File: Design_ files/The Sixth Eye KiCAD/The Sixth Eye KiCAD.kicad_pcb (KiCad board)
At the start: 2 copper layers, 33.5 x 31.6 mm, 13 parts, among them J1 Battery conn, J2 US Sensor conn., J3 Vibration out, U1 ATmega328-AU, U2 LTC3525ISC6-5, Y1 8Mhz

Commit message: Accelrometer pcb
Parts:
- added C5: 2.2uf, Capacitor_Tantalum_SMD:CP_EIA-1608-10_AVX-L, F.Cu at (154.9, 71.9)
- added H2: MountingHole, MountingHole:MountingHole_2mm, F.Cu at (155.7, 65.7)
- added Q1: BC547, Package_TO_SOT_SMD:SOT-23, F.Cu at (148.9, 69.1)
- added R2: 2.2R, Resistor_SMD:R_0603_1608Metric_Pad0.98x0.95mm_HandSolder, F.Cu at (150.2, 74.4)
- added U3: ADXL343, Package_LGA:LGA-14_3x5mm_P0.8mm_LayoutBorder1x6y, F.Cu at (142.6, 68.4)
- added c2: 0.1uf, Capacitor_Tantalum_SMD:CP_EIA-1608-08_AVX-J, F.Cu at (142.4, 64.6)
- moved J2 15.8 mm to (132.4, 67.9), turned to 270 degrees
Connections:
- U1 pad 13: Echo -> Net-(U1-Pad13)
- U1 pad 14: Trig -> ~CS
- U1 pad 15: Net-(U1-Pad15) -> MOSI
- U1 pad 16: Out -> MISO
- U1 pad 17: Net-(U1-Pad17) -> SCK
- U1 pad 23: Net-(U1-Pad23) -> Out
- U1 pad 24: Net-(U1-Pad24) -> Echo
- U1 pad 25: Net-(U1-Pad25) -> Trig
- U1 pad 26: Net-(U1-Pad26) -> VDD_IO
- U1 pad 27: Net-(U1-Pad27) -> INT1
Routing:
- net ~CS: track 0.00 -> 19.8 mm
- net Trig: track 24.0 -> 4.14 mm
- net Net-(U1-Pad13): track 0.00 -> 17.9 mm
- net Echo: track 24.6 -> 6.70 mm
- removed copper zone on B.Cu, net GND
- removed copper zone on F.Cu, net GND
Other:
- board outline removed

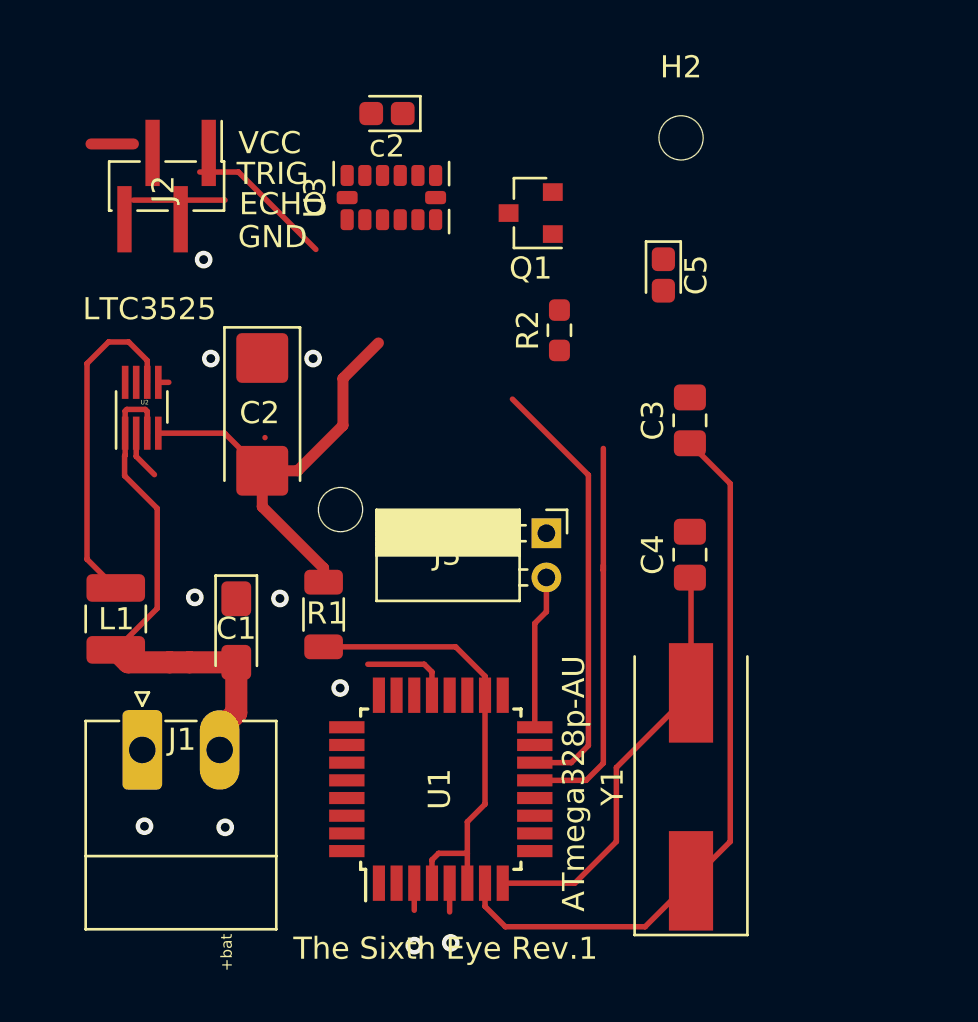
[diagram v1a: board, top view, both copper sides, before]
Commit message: KiCAD Pcb completed for Sixth_Eye including Accelerometer
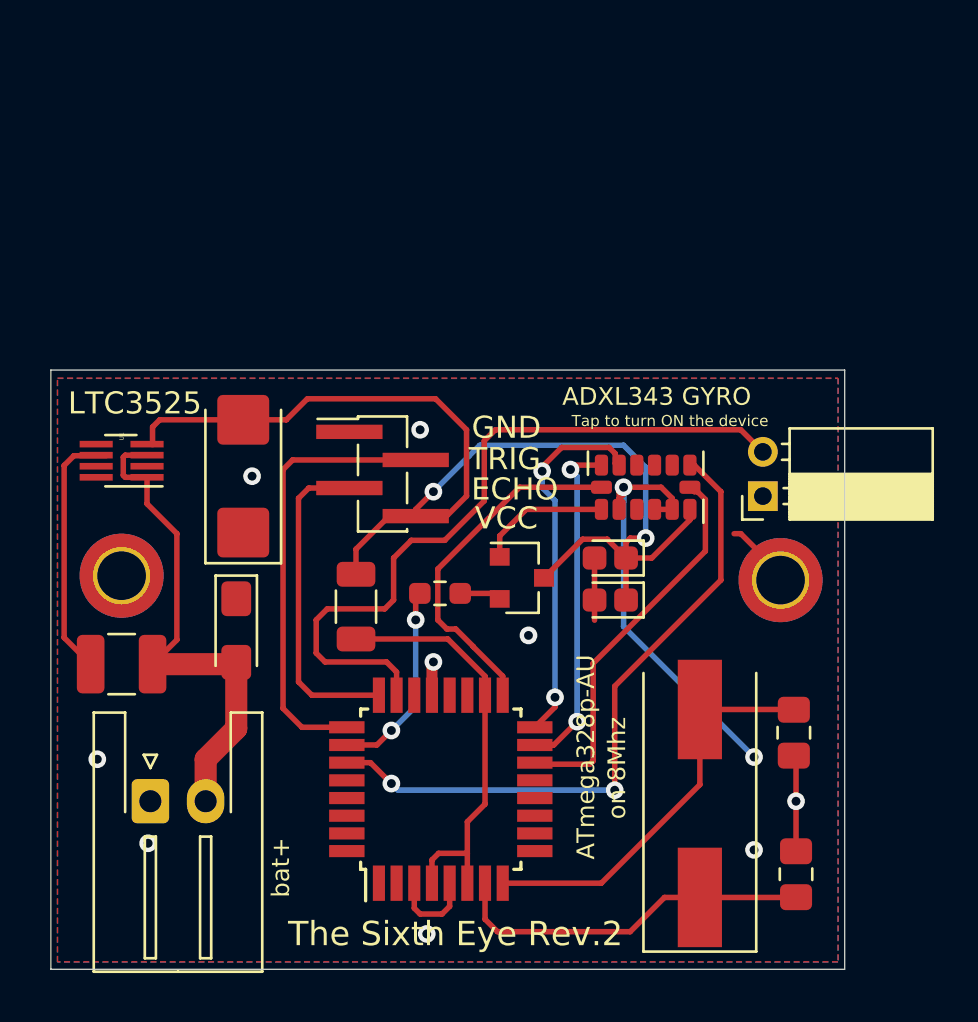
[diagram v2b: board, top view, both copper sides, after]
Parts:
- removed the J1 at (131.3, 93.4)
- removed c2: 0.1uf, Capacitor_Tantalum_SMD:CP_EIA-1608-08_AVX-J
- added C6: 0.1uf, Capacitor_Tantalum_SMD:CP_EIA-1608-08_AVX-J, F.Cu at (152.5, 84.7)
- added J2: Battery conn, Connector_JST:JST_XH_S2B-XH-A-1_1x02_P2.50mm_Horizontal, F.Cu at (131.7, 95.7)
- H1, H2: value MountingHole -> MountingHole_Pad; footprint MountingHole:MountingHole_2mm -> MountingHole:MountingHole_2.2mm_M2_DIN965_Pad_TopBottom
- moved C3 21.1 mm to (160.9, 99.0)
- moved H2 20.5 mm to (160.2, 85.7)
- moved U3 17.4 mm to (154.1, 81.5)
- moved Q1 16.5 mm to (148.5, 85.6), turned to 0 degrees
- moved J3 16.3 mm to (142.2, 80.9), turned to 0 degrees
- moved C5 14.9 mm to (152.5, 86.6), turned to 180 degrees
- moved R2 13.1 mm to (144.8, 86.3), turned to 0 degrees
- moved H1 10.3 mm to (130.4, 85.5)
- moved J1 9.93 mm to (159.4, 81.9), turned to 180 degrees
- moved C4 9.32 mm to (160.8, 92.6), turned to 270 degrees
- moved C2 2.92 mm to (135.9, 81.0), turned to 90 degrees
- moved U1 2.56 mm to (130.4, 80.3), turned to 180 degrees
- moved L1 2.06 mm to (130.4, 89.5), turned to 180 degrees
- moved R1 1.51 mm to (141.0, 86.9)
- moved Y1 0.85 mm to (156.6, 95.8)
- renumbered J3 to J1, J2 to J3, U2 to U1, U1 to U2
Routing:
- net 3.3v: track 22.4 -> 54.2 mm, vias 0 -> 2
- net INT1: track 0.00 -> 30.0 mm, vias 0 -> 2
- net GND: track 9.31 -> 36.9 mm, vias 11 -> 12
- net Out: track 6.99 -> 33.4 mm
- net Net-(U2-Pad13): track 17.9 -> 0.00 mm
- net MISO: track 0.00 -> 16.8 mm, vias 0 -> 2
- net XTAL1: track 32.9 -> 16.6 mm
- net SCK: track 0.00 -> 16.1 mm
- net Trig: track 4.14 -> 20.2 mm
- net MOSI: track 0.00 -> 15.4 mm, vias 0 -> 2
- net VDD_IO: track 0.00 -> 9.02 mm, vias 0 -> 2
- net Echo: track 6.70 -> 14.7 mm
- net Net-(Q1-Pad1): track 0.00 -> 6.05 mm
- net Net-(L1-Pad2): track 15.2 -> 11.6 mm
- net ~CS: track 19.8 -> 17.6 mm
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- added copper zone on B.Cu, net GND
- added copper zone on F.Cu, net GND
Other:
- board outline added: 35.9 x 27.1 mm
- board text added: "ADXL343 GYRO"
- board text added: "Tap to turn ON the device"
- board text added: "The Sixth Eye Rev.2"
- board text added: "bat+"
- board text added: "on 8Mhz"
- board text removed: "+bat"
- board text removed: "The Sixth Eye Rev.1"
